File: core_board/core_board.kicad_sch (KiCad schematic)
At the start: 96 parts

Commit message: last commit before starting layout
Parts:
- removed JP? (x2): Jumper, symbol Jumper:Jumper_2_Open
- added JP?: Jumper_3_Bridged12, symbol Jumper:Jumper_3_Bridged12
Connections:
- net SPI_CS_CORE: now also JP?.2 (C)
- net at R?.1, U?.2 (CS): now also JP?.3 (B)
- net at R?.1, U?.2 (CS): now also JP?.1 (A)

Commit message: created netlist
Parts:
- C1, C2, C3, C4: renamed from C?; footprint (none) -> Capacitor_SMD:C_0603_1608Metric
- D2, D3, D4, D5, D6, D7, D8, D9: renamed from D?; footprint (none) -> LED_SMD:LED_0603_1608Metric
- J1: renamed from J?; footprint (none) -> Ellie_Project_Footprints:DEANS
- J10, J3, J4, J5, J6, J7, J8, J9: renamed from J?; footprint SAMTEC_PCIE-LP-01-01-F-DV-A-TR -> PCIE_Socket:SAMTEC_PCIE-LP-01-01-F-DV-A-TR
- J2: renamed from J?; footprint (none) -> Connector_PinHeader_2.54mm:PinHeader_1x03_P2.54mm_Vertical
- JP1, JP2: renamed from JP?; footprint (none) -> Connector_PinHeader_2.54mm:PinHeader_1x02_P2.54mm_Vertical
- JP3: renamed from JP?; footprint (none) -> Connector_PinHeader_2.54mm:PinHeader_1x03_P2.54mm_Vertical
- R1, R10, R11, R12, R13, R14, R15, R16, R17, R18, R19, R2, R20, R21, R22, R23, R24, R25, R26, R27, R28, R29, R3, R30, R31, R32, R33, R34, R35, R36, R37, R38, R4, R5, R6, R7, R8, R9: renamed from R?; footprint (none) -> Resistor_SMD:R_0603_1608Metric
- SW1, SW2, SW3, SW4, SW5, SW6, SW7, SW8: renamed from SW?; footprint (none) -> Button_Switch_SMD:SW_SPST_PTS810
- TP1, TP10, TP11, TP12, TP13, TP14, TP15, TP16, TP2, TP3, TP4, TP5, TP6, TP7, TP8, TP9: renamed from TP?; footprint (none) -> TestPoint:TestPoint_Plated_Hole_D5.0mm
- U1: renamed from U?; footprint MODULE_ESP32-DEVKITC-32D -> Ellie_Project_Footprints:MODULE_ESP32-DEVKITC-32D
- U2, U3: renamed from U?; footprint TO255P1020X450X1968-3 -> LD1117V33:TO255P1020X450X1968-3
- U4, U5: renamed from U?; footprint (none) -> Ellie_Project_Footprints:SD_Card_Breakout
- U6: renamed from U?; footprint (none) -> PCF8575_Breakout:PCF8575_Breakout
- U7: renamed from U?; footprint (none) -> TCA9548A_Breakout:TCA9548A_Breakout
- gave numbers to parts that had none: 1

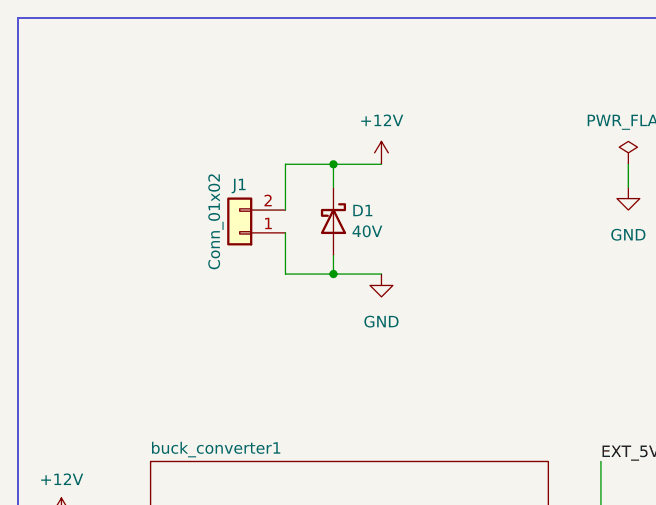
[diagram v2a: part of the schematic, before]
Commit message: did layout, and power routing
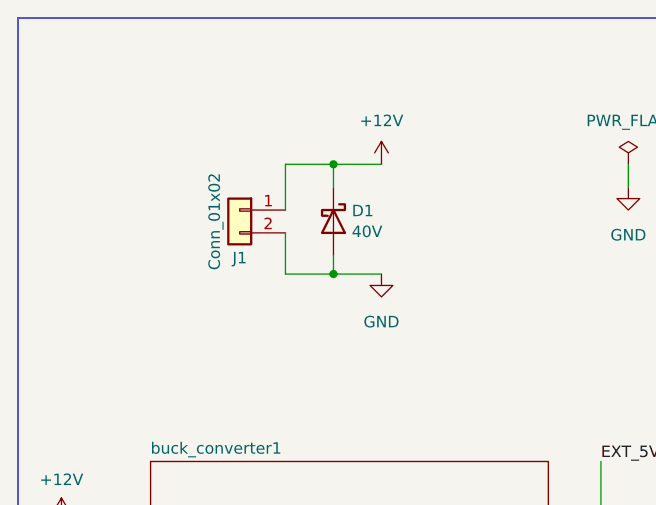
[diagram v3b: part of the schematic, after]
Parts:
- TP1, TP10, TP11, TP12, TP13, TP14, TP15, TP16, TP2, TP3, TP4, TP5, TP6, TP7, TP8, TP9: footprint TestPoint:TestPoint_Plated_Hole_D5.0mm -> TestPoint:TestPoint_Plated_Hole_D2.0mm
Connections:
- net +12V: now also J1.1 (Pin_1); no longer J1.2 (Pin_2)
- net GND: now also J1.2 (Pin_2); no longer J1.1 (Pin_1)
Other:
- moved on the sheet: J1

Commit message: more routing progress
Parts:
- removed TP1, TP2: TestPoint, TestPoint:TestPoint_Plated_Hole_D2.0mm, symbol Connector:TestPoint
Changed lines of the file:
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@@
   (junction (at 162.56 116.078) (diameter 0) (color 0 0 0 0)
   )
-  (junction (at 136.906 257.048) (diameter 0) (color 0 0 0 0)
-  )
   (junction (at 305.054 133.858) (diameter 0) (color 0 0 0 0)
   )
@@
   (junction (at 361.442 57.658) (diameter 0) (color 0 0 0 0)
   )
-  (junction (at 175.768 257.048) (diameter 0) (color 0 0 0 0)
-  )
   (junction (at 303.53 103.378) (diameter 0) (color 0 0 0 0)
   )
@@
     (stroke (width 0) (type default) (color 0 0 0 0))
   )
-  (wire (pts (xy 136.906 257.048) (xy 143.256 257.048))
-    (stroke (width 0) (type default) (color 0 0 0 0))
-  )
   (wire (pts (xy 246.888 62.738) (xy 245.872 62.738))
     (stroke (width 0) (type default) (color 0 0 0 0))
@@
     (stroke (width 0) (type default) (color 0 0 0 0))
   )
-  (wire (pts (xy 175.768 257.048) (xy 182.118 257.048))
-    (stroke (width 0) (type default) (color 0 0 0 0))
-  )
   (wire (pts (xy 193.294 183.134) (xy 193.294 185.674))
     (stroke (width 0) (type default) (color 0 0 0 0))
@@
     (pin "1")
   )
-  (symbol (lib_id "Connector:TestPoint") (at 143.256 257.048 0) (unit 1)
-    (in_bom yes) (on_board yes)
-    (property "Reference" "TP1" (id 0) (at 139.954 248.666 0)
-      (effects (font (size 1.27 1.27)) (justify left))
-    )
-    (property "Value" "TestPoint" (id 1) (at 139.954 251.206 0)
-      (effects (font (size 1.27 1.27)) (justify left))
-    )
-    (property "Footprint" "TestPoint:TestPoint_Plated_Hole_D2.0mm" (id 2) (at 148.336 257.048 0)
-      (effects (font (size 1.27 1.27)) hide)
-    )
-    (property "Datasheet" "~" (id 3) (at 148.336 257.048 0)
-      (effects (font (size 1.27 1.27)) hide)
-    )
-    (pin "1")
-  )
   (symbol (lib_id "power:GND") (at 136.906 276.86 0) (unit 1)
     (in_bom yes) (on_board yes) (fields_autoplaced)
@@
     (pin "1")
   )
-  (symbol (lib_id "Connector:TestPoint") (at 182.118 257.048 0) (unit 1)
-    (in_bom yes) (on_board yes)
-    (property "Reference" "TP2" (id 0) (at 178.816 248.666 0)
-      (effects (font (size 1.27 1.27)) (justify left))
-    )
-    (property "Value" "TestPoint" (id 1) (at 178.816 251.206 0)
-      (effects (font (size 1.27 1.27)) (justify left))
-    )
-    (property "Footprint" "TestPoint:TestPoint_Plated_Hole_D2.0mm" (id 2) (at 187.198 257.048 0)
-      (effects (font (size 1.27 1.27)) hide)
-    )
-    (property "Datasheet" "~" (id 3) (at 187.198 257.048 0)
-      (effects (font (size 1.27 1.27)) hide)
-    )
-    (pin "1")
-  )
   (symbol (lib_id "PCIE_Socket:PCIE-LP-01-01-F-DV-A-TR") (at 176.276 116.078 0) (unit 1)
     (in_bom yes) (on_board yes) (fields_autoplaced)
@@
       (reference "SW8") (unit 1) (value "SW_Push") (footprint "Button_Switch_SMD:SW_SPST_PTS810")
     )
-    (path "/408e23ac-92c0-42b0-943c-19fe687ae4ac"
-      (reference "TP1") (unit 1) (value "TestPoint") (footprint "TestPoint:TestPoint_Plated_Hole_D2.0mm")
-    )
-    (path "/45fbf304-3141-4d25-95fa-f688f12a590d"
-      (reference "TP2") (unit 1) (value "TestPoint") (footprint "TestPoint:TestPoint_Plated_Hole_D2.0mm")
-    )
     (path "/0b607bb8-ba93-4226-b73b-e50e0eee7a8a"
